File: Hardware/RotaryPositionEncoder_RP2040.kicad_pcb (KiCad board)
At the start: 4 copper layers, 74 parts, among them J1 Conn_ABI, J2 Conn_UVW, J4 USB_C_Receptacle_USB2.0, J5 Conn_5VDC, J7 Conn_CAN, J8 Conn_CAN, J9 Conn_01x04_MountingPin, U1 AS5047P, U2 RP2040, U3 M24C02-RMN, U5 TJA1042T, U6 RT9013-33GB, U7 MAX14783ExS, U8 W25Q32JVZP, Y2 Crystal_GND2

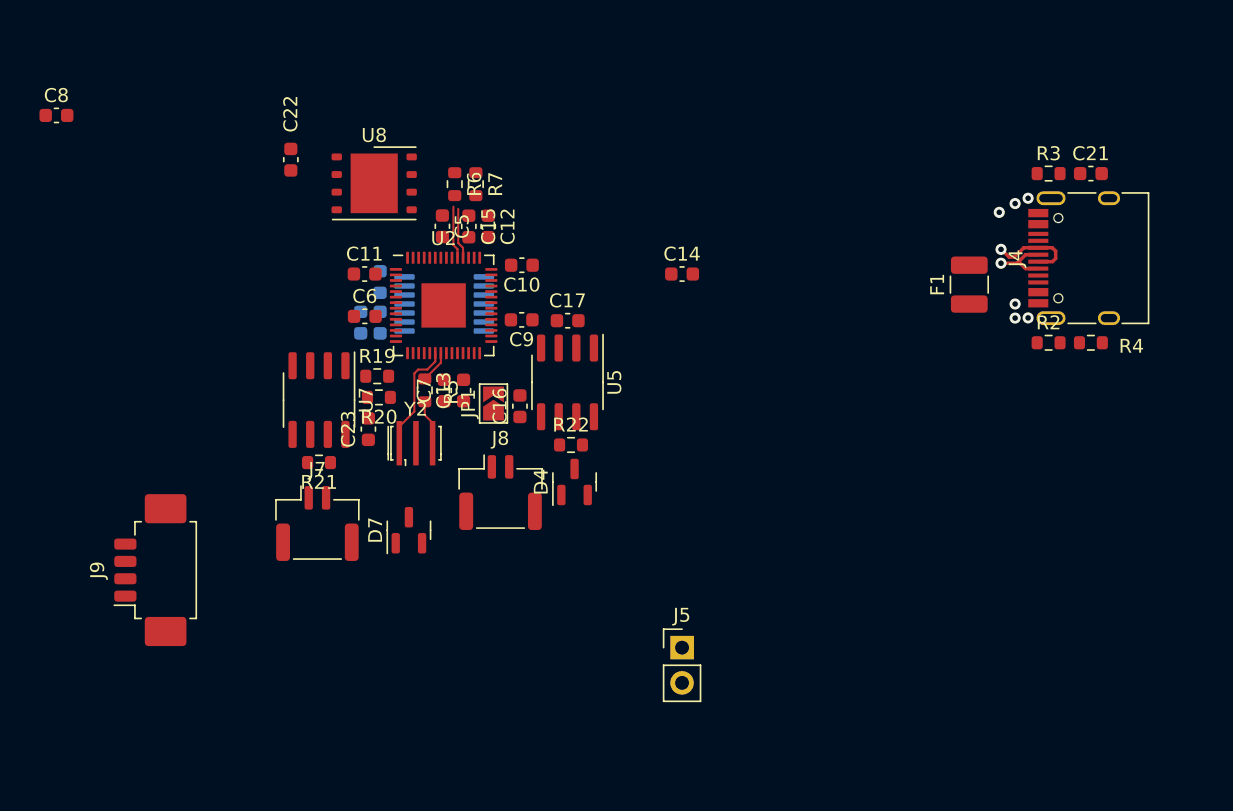
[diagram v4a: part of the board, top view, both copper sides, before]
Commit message: Changed USB-C Plug into GH1.25 Connector to take less space
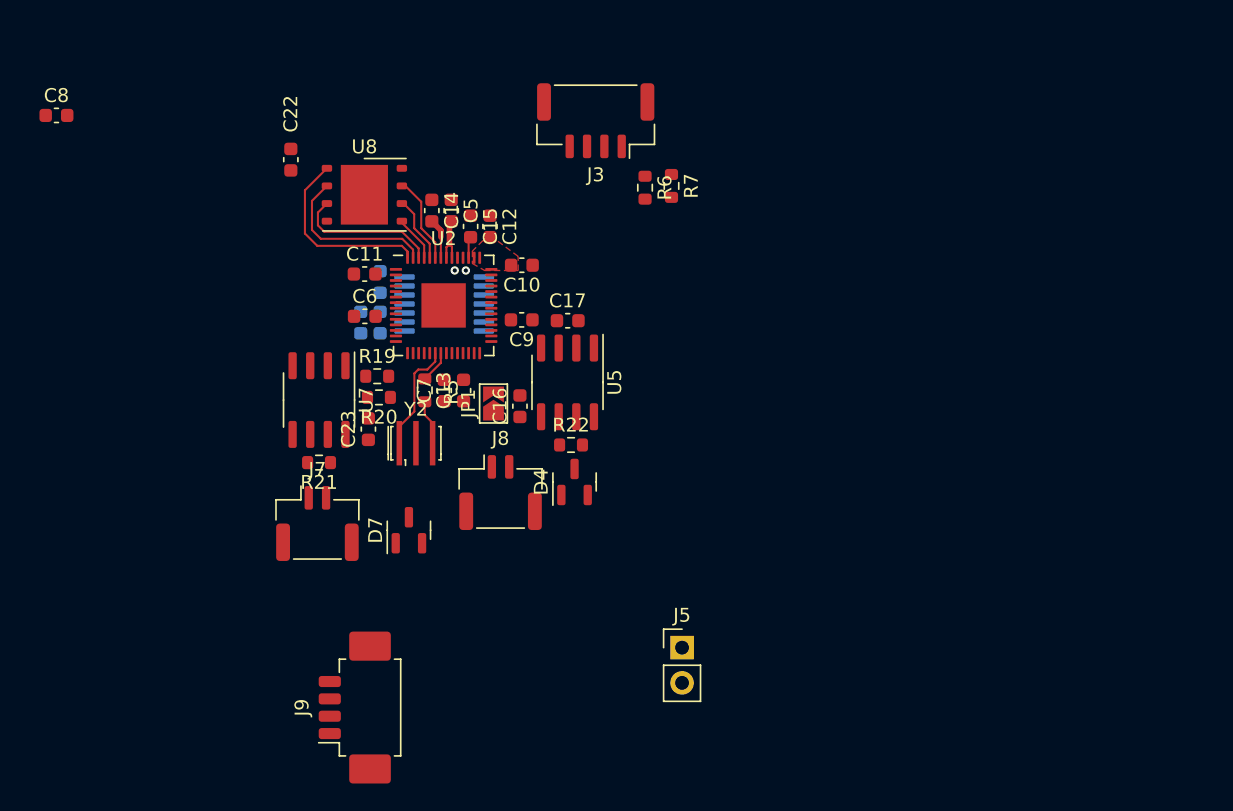
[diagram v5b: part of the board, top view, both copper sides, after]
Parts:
- removed C21: 10nF, Capacitor_SMD:C_0603_1608Metric
- removed F1: Fuse, Fuse:Fuse_1210_3225Metric
- removed J4: USB_C_Receptacle_USB2.0, Connector_USB:USB_C_Receptacle_HRO_TYPE-C-31-M-12
- removed R2, R3: 5.1k, Resistor_SMD:R_0603_1608Metric
- removed R4: 1M, Resistor_SMD:R_0603_1608Metric
- added J3: Conn_USB, Connector_JST:JST_GH_SM04B-GHS-TB_1x04-1MP_P1.25mm_Horizontal, F.Cu at (99.8, 120.8)
- moved C14 18.6 mm to (88.0, 127.3), turned to -90 degrees
- moved J9 17.8 mm to (83.1, 163.1)
- moved R7 14.1 mm to (105.3, 125.5)
- moved R6 13.7 mm to (103.4, 125.6)
- moved C5 1.30 mm to (89.4, 127.3)
- moved U8 1.08 mm to (83.2, 126.1)
- moved C15 0.13 mm to (90.8, 128.4)
- moved C12 0.13 mm to (92.2, 128.4)
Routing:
- net /QSPI_SS: track 0.00 -> 13.7 mm
- net /QSPI_SD1: track 0.00 -> 12.1 mm
- net /QSPI_SD2: track 0.00 -> 10.5 mm
- net /USB_DP: track 6.42 -> 0.00 mm, vias 1 -> 0
- net /QSPI_SD3: track 0.00 -> 6.32 mm
- net /QSPI_CLK: track 0.00 -> 4.81 mm
- net /USB_DM: track 4.65 -> 0.00 mm, vias 1 -> 0
- net /VREG: track 0.00 -> 4.43 mm
- net +3V3: track 0.00 -> 4.17 mm
- net Net-(U2-USB_DP): track 3.81 -> 0.00 mm, vias 0 -> 1
- net Net-(U2-USB_DM): track 3.67 -> 0.00 mm, vias 0 -> 1
- net /QSPI_SD0: track 0.00 -> 3.30 mm
- net GND: vias 6 -> 0
- added copper zone on F.Cu, net +3V3

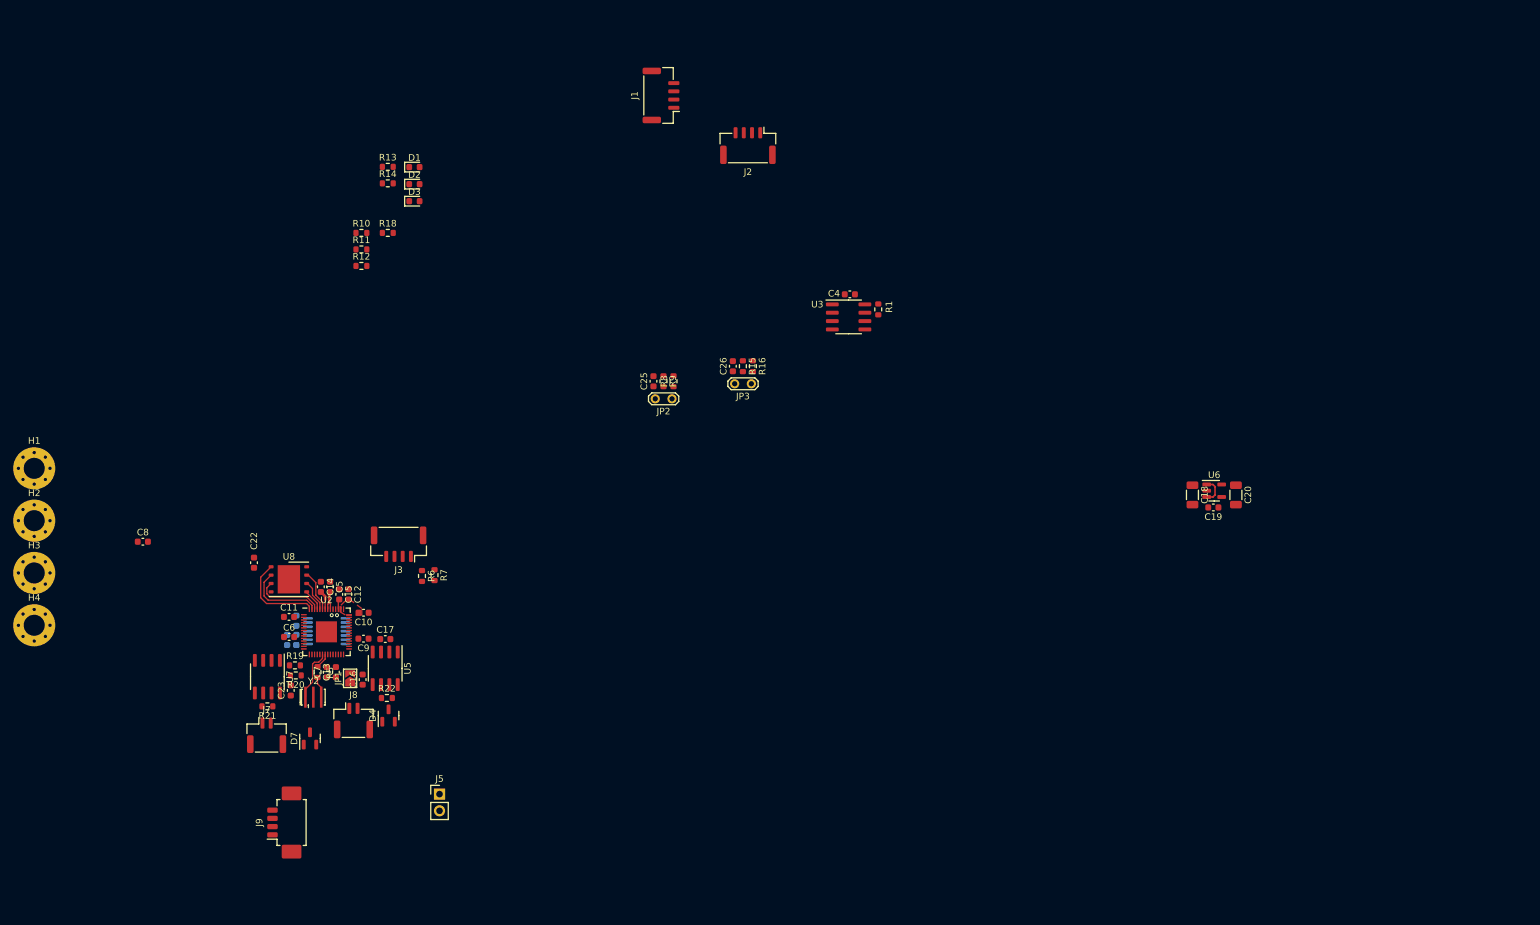
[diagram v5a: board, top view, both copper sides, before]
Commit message: Layout almost done Todo: Change QFN56 footprint into handsolder
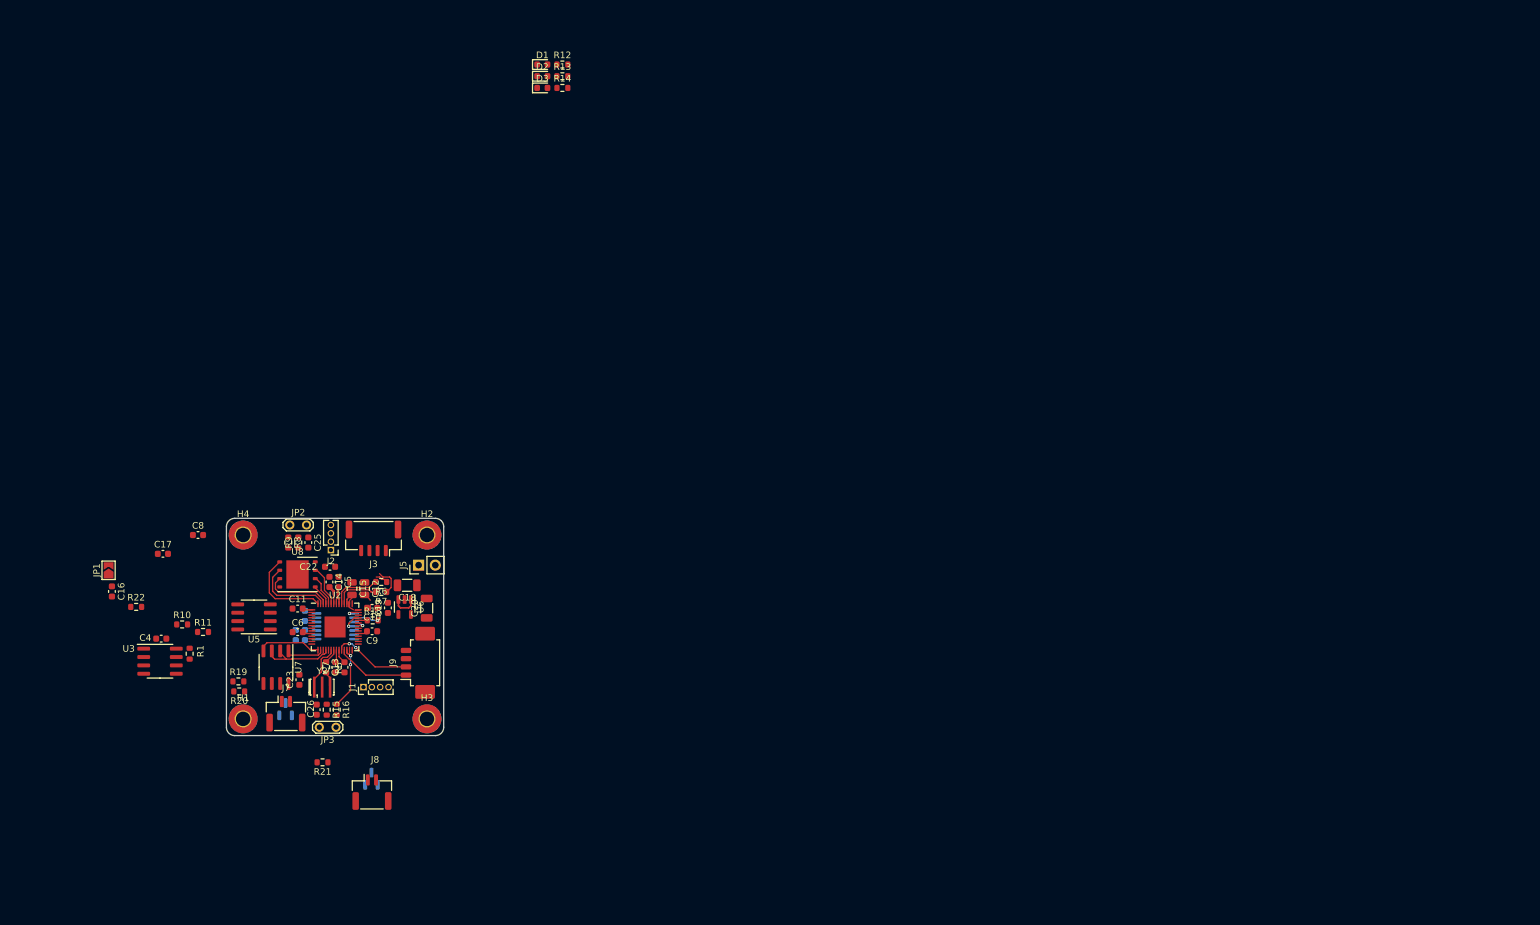
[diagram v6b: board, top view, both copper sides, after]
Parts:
- C12, C15: footprint Capacitor_SMD:C_0603_1608Metric -> Capacitor_SMD:C_0805_2012Metric
- D4, D7: moved to B.Cu
- H1, H2, H3, H4: footprint MountingHole:MountingHole_3.2mm_M3_Pad_Via -> MountingHole:MountingHole_2.2mm_M2_Pad_TopBottom
- J1, J2: footprint Connector_JST:JST_GH_BM04B-GHS-TBT_1x04-1MP_P1.25mm_Vertical -> Connector_PinHeader_1.27mm:PinHeader_1x04_P1.27mm_Vertical
- moved C19 126.4 mm to (98.2, 130.5), turned to 90 degrees
- moved U6 124.3 mm to (100.7, 130.3), turned to -90 degrees
- moved C20 124.2 mm to (104.1, 130.5), turned to 90 degrees
- moved C18 120.1 mm to (101.1, 127.0), turned to 180 degrees
- moved C4 117.0 mm to (63.8, 135.1)
- moved R1 117.0 mm to (68.1, 137.4)
- moved U3 117.0 mm to (63.6, 138.6)
- moved J1 100.6 mm to (94.5, 142.5)
- moved J2 88.3 mm to (89.5, 121.7)
- moved C26 82.0 mm to (87.4, 145.9)
- moved R15 82.0 mm to (88.9, 145.9)
- moved R16 82.0 mm to (90.4, 145.9)
- moved JP3 81.9 mm to (87.8, 148.6)
- moved R10 65.4 mm to (66.9, 133.0)
- moved H3 63.7 mm to (104.1, 147.3)
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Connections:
- R18 pad 1: Net-(U2-GPIO22) -> Net-(U2-GPIO26_ADC0)
- U2 pad 29: unconnected-(U2-GPIO18-Pad29) -> /CAN_TX
- U2 pad 30: /SPI_MOSI -> /CAN_RX
- U2 pad 31: /SPI_MISO -> unconnected-(U2-GPIO20-Pad31)
- U2 pad 32: /SPI_CS -> unconnected-(U2-GPIO21-Pad32)
- U2 pad 34: Net-(U2-GPIO22) -> unconnected-(U2-GPIO22-Pad34)
- U2 pad 36: /CAN_TX -> /SPI_MISO
- U2 pad 37: /CAN_RX -> unconnected-(U2-GPIO25-Pad37)
- U2 pad 38: unconnected-(U2-GPIO26_ADC0-Pad38) -> Net-(U2-GPIO26_ADC0)
- U2 pad 39: unconnected-(U2-GPIO27_ADC1-Pad39) -> /SPI_MOSI
- U2 pad 41: unconnected-(U2-GPIO29_ADC3-Pad41) -> /SPI_CS
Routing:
- net Net-(J9-Pin_2): track 0.00 -> 11.9 mm, vias 0 -> 2
- net Net-(J9-Pin_1): track 0.00 -> 11.4 mm
- net /UART_RTS: track 0.00 -> 11.1 mm
- net /UART_TX: track 0.00 -> 10.3 mm
- net /RUN: track 0.00 -> 9.50 mm, vias 0 -> 2
- net Net-(U2-USB_DP): track 0.00 -> 7.72 mm, vias 1 -> 0
- net Net-(U2-USB_DM): track 0.00 -> 6.91 mm, vias 1 -> 0
- net +3V3: track 4.17 -> 10.3 mm
- net /UART_RX: track 0.00 -> 5.51 mm
- net /USB_DM: track 0.00 -> 4.41 mm
- net /SPI_CLK: track 0.00 -> 3.72 mm, vias 0 -> 1
- net /VREG: track 4.43 -> 7.39 mm
- net /SPI_MOSI: track 0.00 -> 2.77 mm, vias 0 -> 1
- net /SPI_MISO: track 0.00 -> 2.28 mm, vias 0 -> 1
- net /USB_DP: track 0.00 -> 1.90 mm
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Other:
- board outline added: 33 x 33 mm

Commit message: almost done pcb layout v1
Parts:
- removed R12, R13, R14: 4.7K, Resistor_SMD:R_0603_1608Metric
- added R2: 4.7K, Resistor_SMD:R_0603_1608Metric, F.Cu at (97.7, 145.5)
- added R3: 4.7K, Resistor_SMD:R_0603_1608Metric, F.Cu at (97.7, 147.1)
- added R4: 4.7K, Resistor_SMD:R_0603_1608Metric, F.Cu at (97.7, 148.6)
- C16, C4, JP1, R1, U3: moved to B.Cu
- moved D1 101.3 mm to (94.7, 145.5)
- moved D2 101.1 mm to (94.7, 147.1)
- moved D3 100.8 mm to (94.7, 148.6)
- moved J8 37.9 mm to (76.7, 125.7), turned to -90 degrees
- moved D4 36.3 mm to (77.3, 125.1), turned to 0 degrees
- moved JP1 22.4 mm to (77.9, 128.1), turned to 0 degrees
- moved C17 22.0 mm to (83.4, 132.6), turned to -90 degrees
- moved C16 21.6 mm to (77.7, 130.2), turned to 0 degrees
- moved C4 18.7 mm to (81.8, 140.2), turned to -90 degrees
- moved U3 14.7 mm to (78.2, 140.0), turned to 90 degrees
- moved R22 14.6 mm to (74.4, 132.1), turned to -90 degrees
- moved C8 13.1 mm to (61.7, 108.7)
- moved R1 11.5 mm to (79.4, 135.4), turned to 0 degrees
- moved R11 8.56 mm to (62.1, 137.2)
- moved R21 5.34 mm to (82.9, 153.7), turned to 0 degrees
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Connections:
- D4 pad 1: /CAN_L -> /CAN_H
- D4 pad 2: /CAN_H -> /CAN_L
- U2 pad 11: Net-(U2-GPIO8) -> unconnected-(U2-GPIO8-Pad11)
- U2 pad 12: Net-(U2-GPIO9) -> unconnected-(U2-GPIO9-Pad12)
- U2 pad 13: Net-(U2-GPIO10) -> unconnected-(U2-GPIO10-Pad13)
- U2 pad 2: unconnected-(U2-GPIO0-Pad2) -> /CAN_RX
- U2 pad 29: /CAN_TX -> Net-(U2-GPIO18)
- U2 pad 3: unconnected-(U2-GPIO1-Pad3) -> /CAN_TX
- U2 pad 30: /CAN_RX -> Net-(U2-GPIO19)
- U2 pad 31: unconnected-(U2-GPIO20-Pad31) -> Net-(U2-GPIO20)
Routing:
- net Net-(U2-GPIO20): track 0.00 -> 19.8 mm, vias 0 -> 2
- net Net-(U2-GPIO19): track 0.00 -> 15.6 mm, vias 0 -> 2
- net Net-(U2-GPIO18): track 0.00 -> 13.0 mm, vias 0 -> 2
- net /CAN_TX: track 0.00 -> 6.90 mm
- net /CAN_RX: track 0.00 -> 5.63 mm
- net /USB_DP: track 1.90 -> 5.87 mm
- net /USB_DM: track 4.41 -> 8.15 mm
- net /CAN_L: track 0.00 -> 2.90 mm, vias 0 -> 1
- net /UART_RTS: track 11.1 -> 13.4 mm, vias 0 -> 2
- net GND: track 0.00 -> 2.31 mm, vias 0 -> 2
- net /CAN_H: track 0.00 -> 2.25 mm, vias 0 -> 1
- net +5V: track 4.05 -> 6.24 mm
- net /SPI_CS: track 1.31 -> 2.84 mm
- net /QSPI_SS: track 13.5 -> 14.7 mm
- net /QSPI_SD1: track 12.1 -> 13.1 mm
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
